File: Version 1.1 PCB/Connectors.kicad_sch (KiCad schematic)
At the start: 12 parts

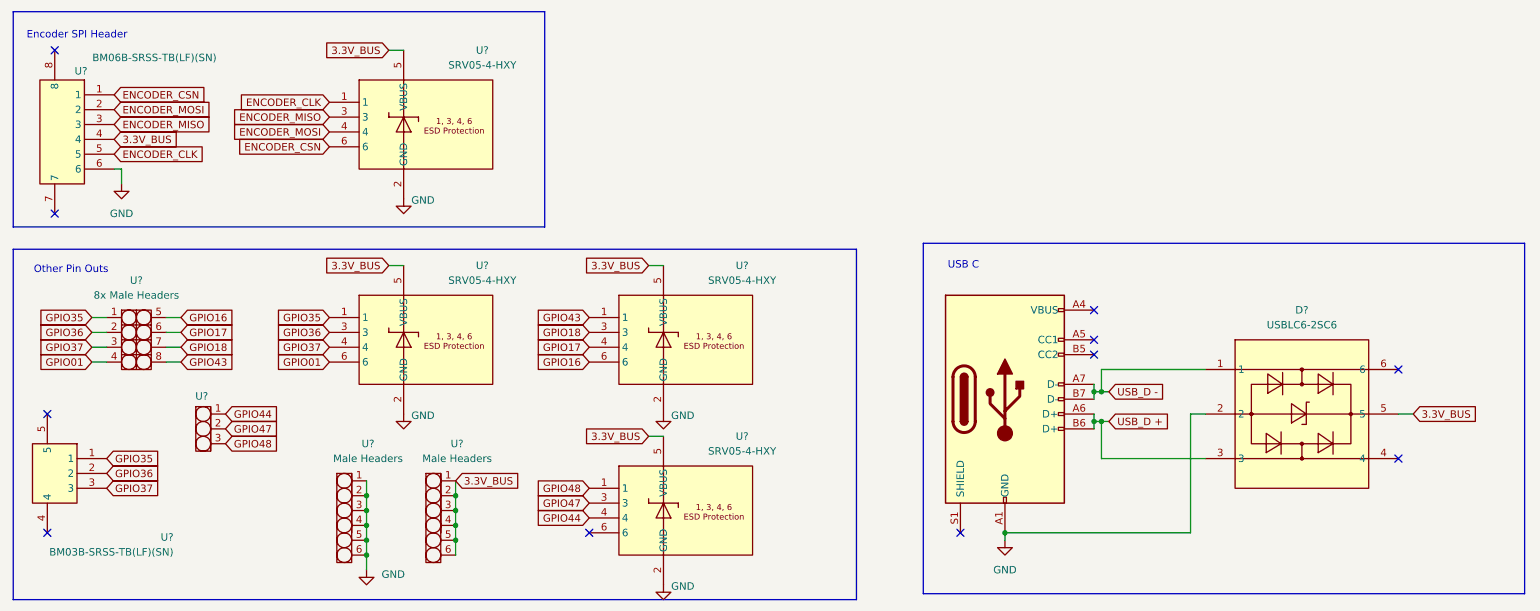
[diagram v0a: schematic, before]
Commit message: began part placement
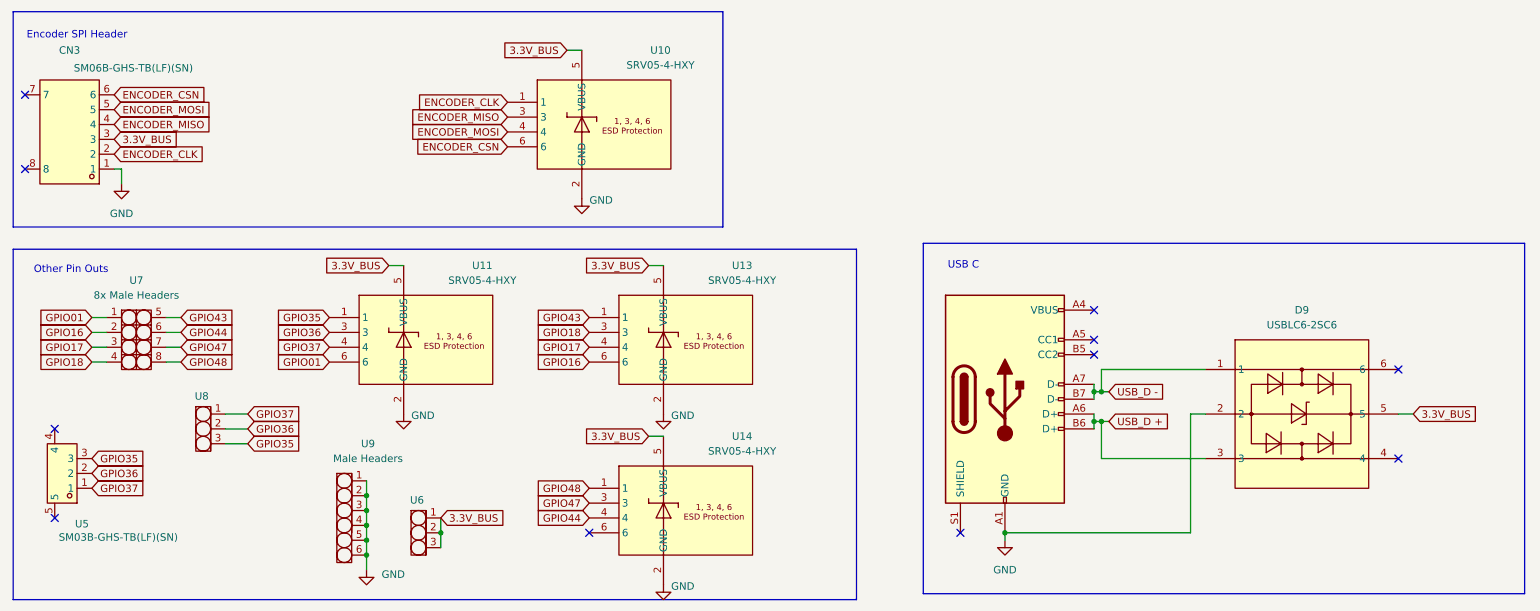
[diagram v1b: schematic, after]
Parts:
- removed U?: BM03B-SRSS-TB(LF)(SN), easyeda2kicad:CONN-SMD-3P-P1.00_BM03B-SRSS-TB-LF-SN, symbol easyeda2kicad:BM03B-SRSS-TB(LF)(SN)
- removed U?: Male Headers, Project_BLDC_Foorprint_Library:1x6 Male Headers, symbol BLDC_Project_Sym_Lib:1x6_Male_Headers
- removed U?: BM06B-SRSS-TB(LF)(SN), easyeda2kicad:CONN-SMD-6P-P1.00_BM06B-SRSS-TB-LF-SN, symbol easyeda2kicad:BM06B-SRSS-TB(LF)(SN)
- added CN3: SM06B-GHS-TB(LF)(SN), easyeda2kicad:CONN-TH_SM06B-GHS-TB-LF-SN, symbol easyeda2kicad:SM06B-GHS-TB(LF)(SN)
- added U5: SM03B-GHS-TB(LF)(SN), easyeda2kicad:CONN-TH_SM03B-GHS-TB-LF-SN, symbol easyeda2kicad:SM03B-GHS-TB(LF)(SN)
- added U6: ~, Project_BLDC_Foorprint_Library:1x3 Male Headers, symbol BLDC_Project_Sym_Lib:1x3_Male_Headers
- J1: renamed from J?; footprint (none) -> easyeda2kicad:USB-C_SMD-TYPE-C-31-M-12
- gave numbers to parts that had none: 8
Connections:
- net 3.3V_BUS: now also CN3.3, U6.1, U6.2, U6.3
- net ENCODER_CLK: now also CN3.2
- net ENCODER_CSN: now also CN3.6
- net ENCODER_MISO: now also CN3.4
- net ENCODER_MOSI: now also CN3.5
- net GND: now also CN3.1
- net GPIO01: now also U7.1; no longer U7.4
- net GPIO16: now also U7.2; no longer U7.5
- net GPIO17: now also U7.3; no longer U7.6
- net GPIO18: now also U7.4; no longer U7.7
- net GPIO35: now also U8.3, U5.3; no longer U7.1
- net GPIO36: now also U8.2, U5.2; no longer U7.2
- net GPIO37: now also U8.1, U5.1; no longer U7.3
- net GPIO43: now also U7.5; no longer U7.8
- net GPIO44: now also U7.6; no longer U8.1
- net GPIO47: now also U7.7; no longer U8.2
- net GPIO48: now also U7.8; no longer U8.3
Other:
- moved on the sheet: U10

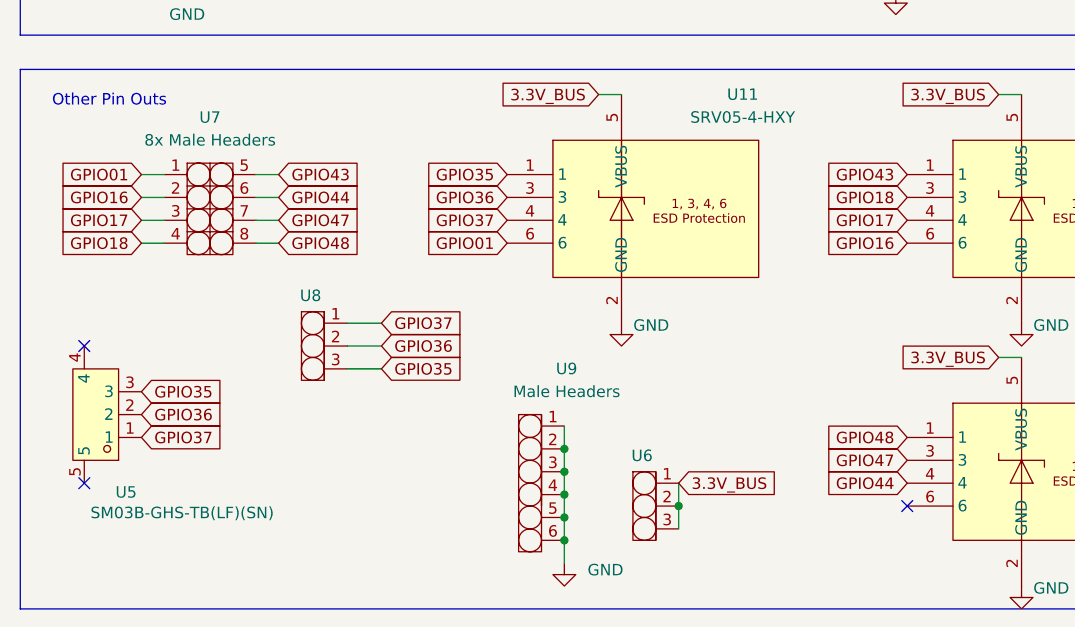
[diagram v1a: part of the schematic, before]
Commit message: Completed Placement of Parts
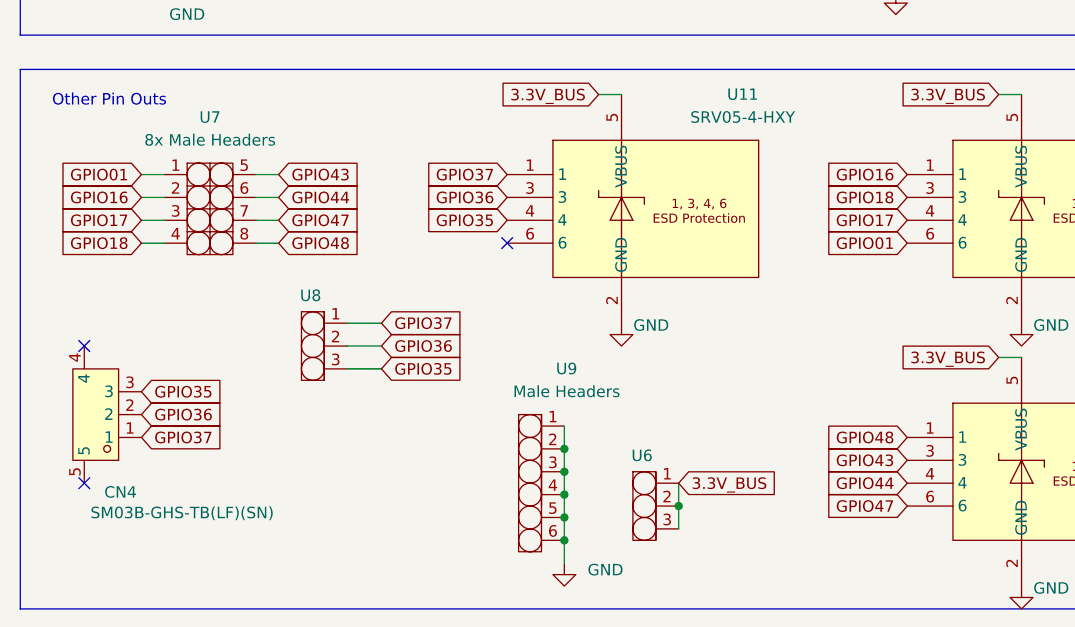
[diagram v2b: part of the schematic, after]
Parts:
- renumbered U5 to CN4
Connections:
- net GPIO01: now also U13.6; no longer U11.6
- net GPIO16: now also U13.1; no longer U13.6
- net GPIO35: now also U11.4; no longer U11.1
- net GPIO37: now also U11.1; no longer U11.4
- net GPIO43: now also U14.3; no longer U13.1
- net GPIO47: now also U14.6; no longer U14.3

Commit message: began working on the routing
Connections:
- net USB_D +: now also D9.1; no longer D9.3
- net USB_D -: now also D9.3; no longer D9.1
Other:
- moved on the sheet: D9
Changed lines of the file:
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@@
-	)
-	(junction
-		(at 203.2 95.25)
-		(diameter 0)
-		(color 0 0 0 0)
 	)
 	(junction
@@
 	)
 	(junction
-		(at 203.2 100.33)
-		(diameter 0)
-		(color 0 0 0 0)
-	)
-	(junction
 		(at 77.47 120.65)
 		(diameter 0)
@@
 	)
 	(no_connect
-		(at 254 91.44)
+		(at 260.35 91.44)
 	)
 	(no_connect
@@
 	)
 	(no_connect
-		(at 254 106.68)
+		(at 260.35 106.68)
 	)
 	(no_connect
@@
 	(wire
 		(pts
-			(xy 254 99.06) (xy 256.54 99.06)
+			(xy 260.35 99.06) (xy 262.89 99.06)
 		)
 		(stroke
@@
 	(wire
 		(pts
-			(xy 203.2 100.33) (xy 203.2 106.68)
-		)
-		(stroke
-			(width 0)
-			(type default)
-		)
-	)
-	(wire
-		(pts
 			(xy 57.15 104.14) (xy 53.34 104.14)
 		)
@@
 	(wire
 		(pts
-			(xy 203.2 95.25) (xy 204.47 95.25)
-		)
-		(stroke
-			(width 0)
-			(type default)
-		)
-	)
-	(wire
-		(pts
 			(xy 77.47 115.57) (xy 77.47 118.11)
 		)
@@
 	(wire
 		(pts
-			(xy 203.2 100.33) (xy 204.47 100.33)
-		)
-		(stroke
-			(width 0)
-			(type default)
-		)
-	)
-	(wire
-		(pts
 			(xy 35.56 57.15) (xy 34.29 57.15)
 		)
@@
 	(wire
 		(pts
-			(xy 201.93 95.25) (xy 203.2 95.25)
+			(xy 201.93 95.25) (xy 204.47 95.25)
+		)
+		(stroke
+			(width 0)
+			(type default)
+		)
+	)
+	(wire
+		(pts
+			(xy 186.69 119.38) (xy 215.9 119.38)
 		)
 		(stroke
@@
 	(wire
 		(pts
-			(xy 203.2 106.68) (xy 220.98 106.68)
-		)
-		(stroke
-			(width 0)
-			(type default)
-		)
-	)
-	(wire
-		(pts
 			(xy 201.93 93.98) (xy 201.93 95.25)
 		)
@@
 	(wire
 		(pts
-			(xy 203.2 91.44) (xy 220.98 91.44)
-		)
-		(stroke
-			(width 0)
-			(type default)
-		)
-	)
-	(wire
-		(pts
 			(xy 186.69 120.65) (xy 186.69 119.38)
 		)
@@
 	(wire
 		(pts
-			(xy 218.44 99.06) (xy 220.98 99.06)
+			(xy 215.9 99.06) (xy 227.33 99.06)
 		)
 		(stroke
@@
 	(wire
 		(pts
-			(xy 218.44 99.06) (xy 218.44 119.38)
-		)
-		(stroke
-			(width 0)
-			(type default)
-		)
-	)
-	(wire
-		(pts
-			(xy 218.44 119.38) (xy 186.69 119.38)
-		)
-		(stroke
-			(width 0)
-			(type default)
-		)
-	)
-	(wire
-		(pts
-			(xy 203.2 95.25) (xy 203.2 91.44)
+			(xy 215.9 99.06) (xy 215.9 119.38)
 		)
 		(stroke
@@
 	(wire
 		(pts
-			(xy 201.93 100.33) (xy 203.2 100.33)
+			(xy 201.93 100.33) (xy 204.47 100.33)
 		)
 		(stroke
@@
 		)
 	)
+	(global_label "USB_D +"
+		(shape input)
+		(at 227.33 91.44 180)
+		(fields_autoplaced yes)
+		(effects
+			(font
+				(size 1.27 1.27)
+			)
+			(justify right)
+		)
+		(property "Intersheetrefs" "${INTERSHEET_REFS}"
+			(at 215.7572 91.44 0)
+			(effects
+				(font
+					(size 1.27 1.27)
+				)
+				(justify right)
+				(hide yes)
+			)
+		)
+	)
 	(global_label "ENCODER_CLK"
 		(shape input)
@@
 	(global_label "3.3V_BUS"
 		(shape input)
-		(at 256.54 99.06 0)
-		(fields_autoplaced yes)
-		(effects
-			(font
-				(size 1.27 1.27)
-			)
-			(justify left)
-		)
-		(property "Intersheetrefs" "${INTERSHEET_REFS}"
-			(at 268.4152 99.06 0)
+		(at 262.89 99.06 0)
+		(fields_autoplaced yes)
+		(effects
+			(font
+				(size 1.27 1.27)
+			)
+			(justify left)
+		)
+		(property "Intersheetrefs" "${INTERSHEET_REFS}"
+			(at 274.7652 99.06 0)
 			(effects
 				(font
@@
 		(property "Intersheetrefs" "${INTERSHEET_REFS}"
 			(at 105.6905 116.84 0)
+			(effects
+				(font
+					(size 1.27 1.27)
+				)
+				(justify right)
+				(hide yes)
+			)
+		)
+	)
+	(global_label "USB_D -"
+		(shape input)
+		(at 227.33 106.68 180)
+		(fields_autoplaced yes)
+		(effects
+			(font
+				(size 1.27 1.27)
+			)
+			(justify right)
+		)
+		(property "Intersheetrefs" "${INTERSHEET_REFS}"
+			(at 215.7572 106.68 0)
 			(effects
 				(font
@@
 	(symbol
 		(lib_id "easyeda2kicad:USBLC6-2SC6")
-		(at 237.49 99.06 0)
+		(at 243.84 99.06 0)
 		(unit 1)
 		(exclude_from_sim no)
@@
 		(fields_autoplaced yes)
 		(property "Reference" "D9"
-			(at 237.49 81.28 0)
+			(at 243.84 81.28 0)
 			(effects
 				(font
@@
 		)
 		(property "Value" "USBLC6-2SC6"
-			(at 237.49 83.82 0)
+			(at 243.84 83.82 0)
 			(effects
 				(font
@@
 		)
 		(property "Footprint" "easyeda2kicad:SOT-23-6_L2.9-W1.6-P0.95-LS2.8-BL"
-			(at 237.49 114.3 0)
+			(at 243.84 114.3 0)
 			(effects
 				(font
@@
 		)
 		(property "Datasheet" "https://lcsc.com/product-detail/Diodes-ESD_STMicroelectronics_USBLC6-2SC6_USBLC6-2SC6_C7519.html"
-			(at 237.49 116.84 0)
+			(at 243.84 116.84 0)
 			(effects
 				(font
@@
 		)
 		(property "Description" ""
-			(at 237.49 99.06 0)
+			(at 243.84 99.06 0)
 			(effects
 				(font
@@
 		)
 		(property "LCSC Part" "C7519"
-			(at 237.49 119.38 0)
+			(at 243.84 119.38 0)
 			(effects
 				(font
@@
 		)
 		(property "Sim.Device" ""
-			(at 237.49 99.06 0)
+			(at 243.84 99.06 0)
 			(effects
 				(font
@@
 		)
 		(property "Sim.Type" ""
-			(at 237.49 99.06 0)
-			(effects
-				(font
+			(at 243.84 99.06 0)
+			(effects
+				(font
